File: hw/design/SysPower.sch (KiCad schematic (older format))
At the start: 14 parts

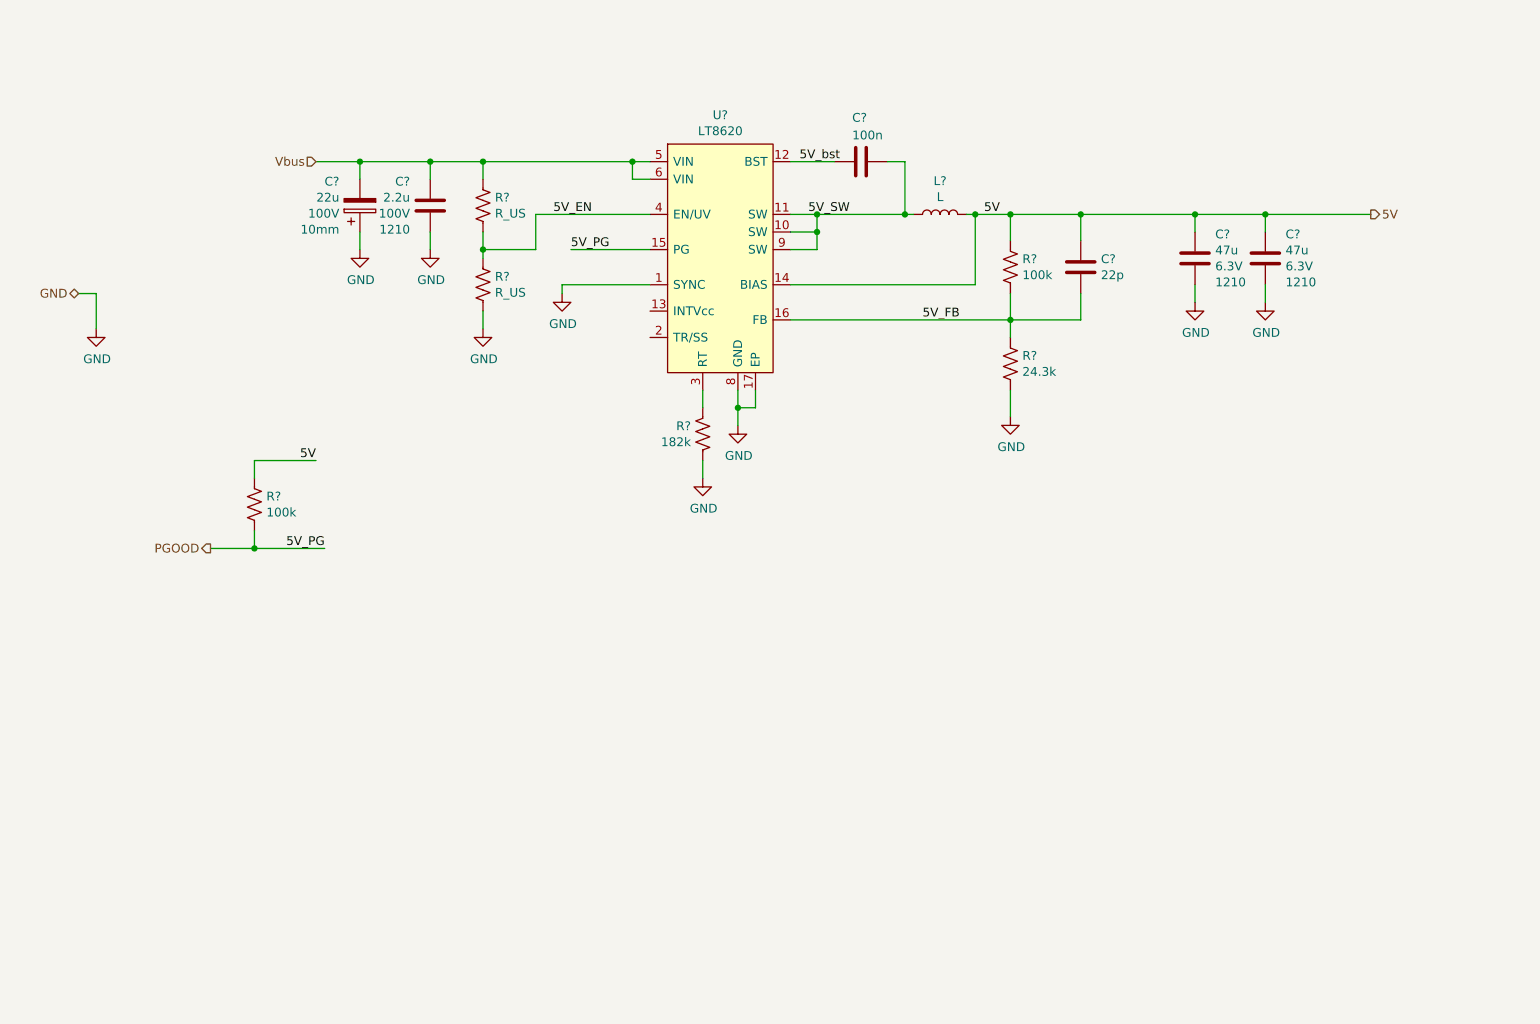
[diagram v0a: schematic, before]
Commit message: reworked adjusters
new V/I adjustment scheme; modified LDO circuit to match
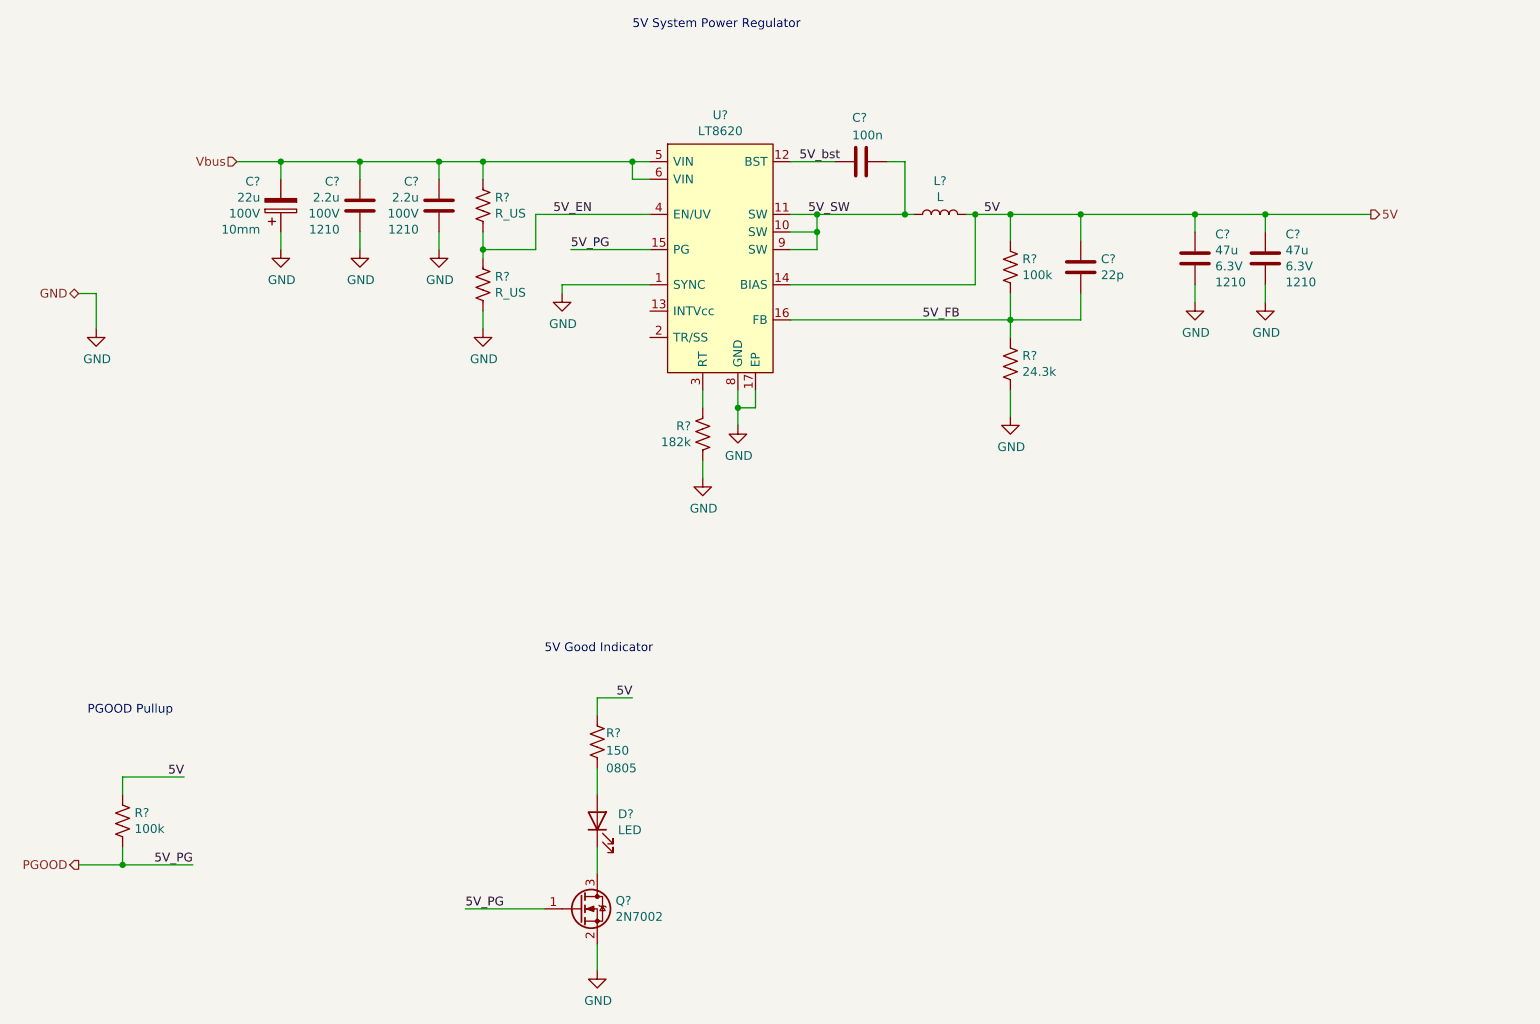
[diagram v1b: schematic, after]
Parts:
- added C?: 2.2u, Capacitor_SMD:C_1210_3225Metric_Pad1.42x2.65mm_HandSolder, symbol Device:C
- added D?: LED, symbol Device:LED
- added Q?: 2N7002, Package_TO_SOT_SMD:SOT-23, symbol Transistor_FET:2N7002
- added R?: 150, Resistor_SMD:R_1206_3216Metric, symbol Device:R_US
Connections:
- net 5V: now also R?.1
- net GND: now also C?.1, Q?.2 (S)
- net PGOOD: now also Q?.1 (G)
- net Vbus: now also C?.2
- new net: D?.2 (A), R?.2
- new net: D?.1 (K), Q?.3 (D)
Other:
- note added: "5V Good Indicator"
- note added: "5V System Power Regulator"
- note added: "PGOOD Pullup"
- moved on the sheet: C?, R?
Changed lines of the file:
@@
 encoding utf-8
 Sheet 7 7
-Title ""
-Date ""
-Rev ""
-Comp ""
-Comment1 ""
+Title "5V System Power"
+Date "2021-02-15"
+Rev "0"
+Comp "The Smith Empire"
+Comment1 "60V input, 5V 2A output"
 Comment2 ""
 Comment3 ""
 Comment4 ""
 $EndDescr
-Text HLabel 3050 2250 0    50   Input ~ 0
+Text HLabel 2600 2250 0    50   Input ~ 0
 Vbus
 Text HLabel 1700 3000 0    50   BiDi ~ 0
 GND
-Text HLabel 2450 4450 0    50   Output ~ 0
+Text HLabel 1700 6250 0    50   Output ~ 0
 PGOOD
 Text HLabel 9050 2550 2    50   Output ~ 0
@@
 L Device:CP C?
 U 1 1 60458D17
-P 3300 2500
-F 0 "C?" H 3183 2363 50  0000 R CNN
-F 1 "22u" H 3183 2454 50  0000 R CNN
-F 2 "" H 3338 2350 50  0001 C CNN
-F 3 "~" H 3300 2500 50  0001 C CNN
-F 4 "Panasonic_100SXV22M" H 3300 2500 50  0001 C CNN "MfrNum"
-F 5 "100V" H 3183 2545 50  0000 R CNN "VRating"
-F 6 "10mm" H 3183 2636 50  0000 R CNN "Size"
-	1    3300 2500
+P 2850 2500
+F 0 "C?" H 2733 2363 50  0000 R CNN
+F 1 "22u" H 2733 2454 50  0000 R CNN
+F 2 "" H 2888 2350 50  0001 C CNN
+F 3 "~" H 2850 2500 50  0001 C CNN
+F 4 "Panasonic_100SXV22M" H 2850 2500 50  0001 C CNN "MfrNum"
+F 5 "100V" H 2733 2545 50  0000 R CNN "VRating"
+F 6 "10mm" H 2733 2636 50  0000 R CNN "Size"
+	1    2850 2500
 	1    0    0    1
 $EndComp
@@
 	4950 2250 4850 2250
 Wire Wire Line
-	3300 2350 3300 2250
-Connection ~ 3300 2250
-Wire Wire Line
-	3300 2250 3050 2250
+	2850 2350 2850 2250
+Connection ~ 2850 2250
+Wire Wire Line
+	2850 2250 2600 2250
 $Comp
 L power:GND #PWR?
 U 1 1 60459F6C
-P 3300 2750
+P 2850 2750
 AR Path="/60459F6C" Ref="#PWR?"  Part="1"
 AR Path="/604399F3/60459F6C" Ref="#PWR?"  Part="1"
-F 0 "#PWR?" H 3300 2500 50  0001 C CNN
-F 1 "GND" H 3305 2577 50  0000 C CNN
-F 2 "" H 3300 2750 50  0001 C CNN
-F 3 "" H 3300 2750 50  0001 C CNN
-	1    3300 2750
-	1    0    0    -1
-$EndComp
-Wire Wire Line
-	3300 2750 3300 2650
+F 0 "#PWR?" H 2850 2500 50  0001 C CNN
+F 1 "GND" H 2855 2577 50  0000 C CNN
+F 2 "" H 2850 2750 50  0001 C CNN
+F 3 "" H 2850 2750 50  0001 C CNN
+	1    2850 2750
+	1    0    0    -1
+$EndComp
+Wire Wire Line
+	2850 2750 2850 2650
 Wire Wire Line
 	4950 2350 4850 2350
@@
 	4000 2750 4000 2800
 Wire Wire Line
-	4000 2250 3700 2250
-Wire Wire Line
-	3700 2750 3700 2650
+	4000 2250 3750 2250
+Wire Wire Line
+	3300 2750 3300 2650
 $Comp
 L power:GND #PWR?
 U 1 1 6045A24A
-P 3700 2750
+P 3300 2750
 AR Path="/6045A24A" Ref="#PWR?"  Part="1"
 AR Path="/604399F3/6045A24A" Ref="#PWR?"  Part="1"
-F 0 "#PWR?" H 3700 2500 50  0001 C CNN
-F 1 "GND" H 3705 2577 50  0000 C CNN
-F 2 "" H 3700 2750 50  0001 C CNN
-F 3 "" H 3700 2750 50  0001 C CNN
-	1    3700 2750
-	1    0    0    -1
-$EndComp
-Wire Wire Line
-	3700 2250 3300 2250
-Connection ~ 3700 2250
-Wire Wire Line
-	3700 2350 3700 2250
+F 0 "#PWR?" H 3300 2500 50  0001 C CNN
+F 1 "GND" H 3305 2577 50  0000 C CNN
+F 2 "" H 3300 2750 50  0001 C CNN
+F 3 "" H 3300 2750 50  0001 C CNN
+	1    3300 2750
+	1    0    0    -1
+$EndComp
+Wire Wire Line
+	3300 2250 2850 2250
+Connection ~ 3300 2250
+Wire Wire Line
+	3300 2350 3300 2250
 $Comp
 L Device:C C?
 U 1 1 60455969
-P 3700 2500
+P 3300 2500
 AR Path="/5EB6CA11/60455969" Ref="C?"  Part="1"
 AR Path="/604399F3/60455969" Ref="C?"  Part="1"
-F 0 "C?" H 3585 2363 50  0000 R CNN
-F 1 "2.2u" H 3585 2454 50  0000 R CNN
-F 2 "Capacitor_SMD:C_1210_3225Metric_Pad1.42x2.65mm_HandSolder" H 3738 2350 50  0001 C CNN
-F 3 "~" H 3700 2500 50  0001 C CNN
-F 4 "TDK_C3225X7R2A225K230AB" H 3700 2500 50  0001 C CNN "MfrNum"
-F 5 "100V" H 3585 2545 50  0000 R CNN "VRating"
-F 6 "1210" H 3585 2636 50  0000 R CNN "Size"
-	1    3700 2500
+F 0 "C?" H 3185 2363 50  0000 R CNN
+F 1 "2.2u" H 3185 2454 50  0000 R CNN
+F 2 "Capacitor_SMD:C_1210_3225Metric_Pad1.42x2.65mm_HandSolder" H 3338 2350 50  0001 C CNN
+F 3 "~" H 3300 2500 50  0001 C CNN
+F 4 "TDK_C3225X7R2A225K230AB" H 3300 2500 50  0001 C CNN "MfrNum"
+F 5 "100V" H 3185 2545 50  0000 R CNN "VRating"
+F 6 "1210" H 3185 2636 50  0000 R CNN "Size"
+	1    3300 2500
 	1    0    0    1
 $EndComp
@@
 L Device:R_US R?
 U 1 1 60476D5E
-P 2700 4200
-F 0 "R?" H 2768 4246 50  0000 L CNN
-F 1 "100k" H 2768 4155 50  0000 L CNN
-F 2 "Resistor_SMD:R_0603_1608Metric" V 2740 4190 50  0001 C CNN
-F 3 "~" H 2700 4200 50  0001 C CNN
-F 4 "0402" H 2768 4109 50  0001 L CNN "Size"
-	1    2700 4200
-	1    0    0    -1
-$EndComp
-Wire Wire Line
-	2700 4350 2700 4450
-Wire Wire Line
-	2700 4450 2450 4450
-Wire Wire Line
-	2700 4450 3100 4450
-Connection ~ 2700 4450
-Text Label 3100 4450 2    50   ~ 0
+P 1950 6000
+F 0 "R?" H 2018 6046 50  0000 L CNN
+F 1 "100k" H 2018 5955 50  0000 L CNN
+F 2 "Resistor_SMD:R_0603_1608Metric" V 1990 5990 50  0001 C CNN
+F 3 "~" H 1950 6000 50  0001 C CNN
+F 4 "0402" H 2018 5909 50  0001 L CNN "Size"
+	1    1950 6000
+	1    0    0    -1
+$EndComp
+Wire Wire Line
+	1950 6150 1950 6250
+Wire Wire Line
+	1950 6250 1700 6250
+Wire Wire Line
+	1950 6250 2350 6250
+Connection ~ 1950 6250
+Text Label 2350 6250 2    50   ~ 0
 5V_PG
 Wire Wire Line
-	2700 4050 2700 3950
-Wire Wire Line
-	2700 3950 3050 3950
-Text Label 3050 3950 2    50   ~ 0
+	1950 5850 1950 5750
+Wire Wire Line
+	1950 5750 2300 5750
+Text Label 2300 5750 2    50   ~ 0
 5V
 $Comp
@@
 Wire Wire Line
 	4450 2950 4450 3000
+$Comp
+L Device:R_US R?
+U 1 1 6035FE45
+P 4650 5550
+F 0 "R?" H 4700 5600 50  0000 L CNN
+F 1 "150" H 4700 5500 50  0000 L CNN
+F 2 "Resistor_SMD:R_1206_3216Metric" V 4690 5540 50  0001 C CNN
+F 3 "~" H 4650 5550 50  0001 C CNN
+F 4 "0805" H 4700 5400 50  0000 L CNN "Size"
+	1    4650 5550
+	1    0    0    -1
+$EndComp
+$Comp
+L Device:LED D?
+U 1 1 60360467
+P 4650 6000
+F 0 "D?" V 4689 5882 50  0000 R CNN
+F 1 "LED" V 4598 5882 50  0000 R CNN
+F 2 "" H 4650 6000 50  0001 C CNN
+F 3 "~" H 4650 6000 50  0001 C CNN
+	1    4650 6000
+	0    -1   -1   0
+$EndComp
+Wire Wire Line
+	4650 5850 4650 5700
+Wire Wire Line
+	4650 5400 4650 5300
+Wire Wire Line
+	4650 5300 4850 5300
+Text Label 4850 5300 2    50   ~ 0
+5V
+$Comp
+L Transistor_FET:2N7002 Q?
+U 1 1 60363BD0
+P 4550 6500
+F 0 "Q?" H 4754 6546 50  0000 L CNN
+F 1 "2N7002" H 4754 6455 50  0000 L CNN
+F 2 "Package_TO_SOT_SMD:SOT-23" H 4750 6425 50  0001 L CIN
+F 3 "https://www.fairchildsemi.com/datasheets/2N/2N7002.pdf" H 4550 6500 50  0001 L CNN
+	1    4550 6500
+	1    0    0    -1
+$EndComp
+Wire Wire Line
+	4650 6150 4650 6300
+$Comp
+L power:GND #PWR?
+U 1 1 6036777D
+P 4650 6850
+AR Path="/6036777D" Ref="#PWR?"  Part="1"
+AR Path="/604399F3/6036777D" Ref="#PWR?"  Part="1"
+F 0 "#PWR?" H 4650 6600 50  0001 C CNN
+F 1 "GND" H 4655 6677 50  0000 C CNN
+F 2 "" H 4650 6850 50  0001 C CNN
+F 3 "" H 4650 6850 50  0001 C CNN
+	1    4650 6850
+	1    0    0    -1
+$EndComp
+Wire Wire Line
+	4650 6850 4650 6700
+Wire Wire Line
+	4350 6500 3900 6500
+Text Label 3900 6500 0    50   ~ 0
+5V_PG
+Text Notes 1750 5400 0    50   ~ 0
+PGOOD Pullup
+Text Notes 4350 5050 0    50   ~ 0
+5V Good Indicator
+Text Notes 4850 1500 0    50   ~ 0
+5V System Power Regulator
+$Comp
+L Device:C C?
+U 1 1 60374DD8
+P 3750 2500
+AR Path="/5EB6CA11/60374DD8" Ref="C?"  Part="1"
+AR Path="/604399F3/60374DD8" Ref="C?"  Part="1"
+F 0 "C?" H 3635 2363 50  0000 R CNN
+F 1 "2.2u" H 3635 2454 50  0000 R CNN
+F 2 "Capacitor_SMD:C_1210_3225Metric_Pad1.42x2.65mm_HandSolder" H 3788 2350 50  0001 C CNN
+F 3 "~" H 3750 2500 50  0001 C CNN
+F 4 "TDK_C3225X7R2A225K230AB" H 3750 2500 50  0001 C CNN "MfrNum"
+F 5 "100V" H 3635 2545 50  0000 R CNN "VRating"
+F 6 "1210" H 3635 2636 50  0000 R CNN "Size"
+	1    3750 2500
+	1    0    0    1
+$EndComp
+Wire Wire Line
+	3750 2350 3750 2250
+Connection ~ 3750 2250
+Wire Wire Line
+	3750 2250 3300 2250
+$Comp
+L power:GND #PWR?
+U 1 1 60376958
+P 3750 2750
+AR Path="/60376958" Ref="#PWR?"  Part="1"
+AR Path="/604399F3/60376958" Ref="#PWR?"  Part="1"
+F 0 "#PWR?" H 3750 2500 50  0001 C CNN
+F 1 "GND" H 3755 2577 50  0000 C CNN
+F 2 "" H 3750 2750 50  0001 C CNN
+F 3 "" H 3750 2750 50  0001 C CNN
+	1    3750 2750
+	1    0    0    -1
+$EndComp
+Wire Wire Line
+	3750 2750 3750 2650
 $EndSCHEMATC

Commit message: label/net reorg, primary SW starting
some reorganization of top-level naming for nets and hierarchical pins

fixed a few part selection issues

started on primary switcher sheet
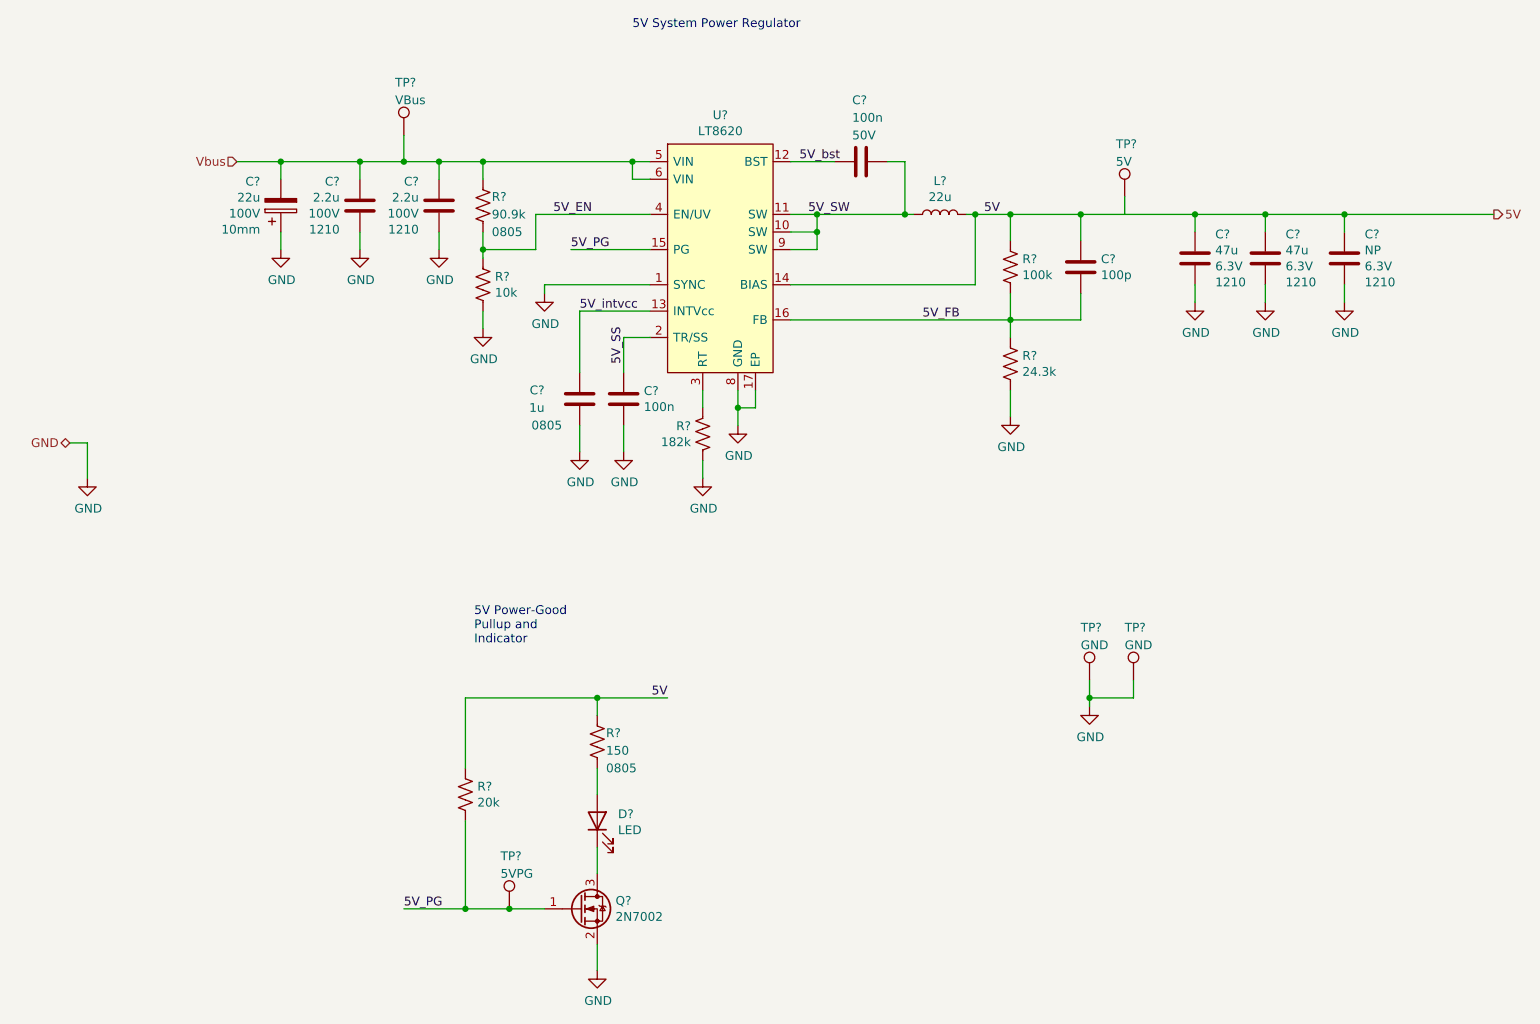
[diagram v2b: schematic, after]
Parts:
- added C?: 100n, Resistor_SMD:R_0603_1608Metric, symbol Device:C
- added C?: 1u, Resistor_SMD:R_0805_2012Metric_Pad1.15x1.40mm_HandSolder, symbol Device:C
- added C?: NP, Capacitor_SMD:C_1210_3225Metric_Pad1.42x2.65mm_HandSolder, symbol Device:C
- added TP?: 5V, TestPoint:TestPoint_Keystone_5000-5004_Miniature, symbol Connector:TestPoint
- added TP?: 5VPG, TestPoint:TestPoint_Keystone_5000-5004_Miniature, symbol Connector:TestPoint
- added TP?: VBus, TestPoint:TestPoint_Keystone_5000-5004_Miniature, symbol Connector:TestPoint
- added TP? (x2): GND, TestPoint:TestPoint_Keystone_5000-5004_Miniature, symbol Connector:TestPoint
- C?: MfrNum TDK_CGA2B2X5R1C104K050BA -> Murata_GRM155R61H104KE19; VRating 16V -> 50V
- C?: value 22p -> 100p
- L?: value L -> 22u; footprint (none) -> Inductor_SMD:L_Vishay_IHLP-4040; MfrNum (none) -> Vishay_IHLP4040DZER220M11
- R?: value R_US -> 90.9k; footprint Resistor_SMD:R_0805_2012Metric -> Resistor_SMD:R_0805_2012Metric_Pad1.15x1.40mm_HandSolder; Size 0603 -> 0805
- R?: value R_US -> 10k
- R?: value 100k -> 20k
- U?: MfrNum (none) -> ADI_LT8620EMSE
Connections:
- net 5V: now also C?.1
- net GND: now also C?.2, C?.2, C?.2, TP?.1, TP?.1
- net Vbus: now also TP?.1
- net 5V_intvcc: now reaches U?.13 (INTVcc)
- net 5V_intvcc: now also C?.1
- net 5V_SS: now reaches U?.2 (TR/SS)
- net 5V_SS: now also C?.1
- net PGOOD renamed 5V_PG
- net 5V_PG: now also TP?.1
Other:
- note added: "5V Power-Good\nPullup and\nIndicator"
- note removed: "5V Good Indicator"
- note removed: "PGOOD Pullup"
- moved on the sheet: R?
